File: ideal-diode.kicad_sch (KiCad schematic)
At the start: 6 parts, among them Q1 SIS472DN-T1-GE3, U6 LM74700QDBVRQ1

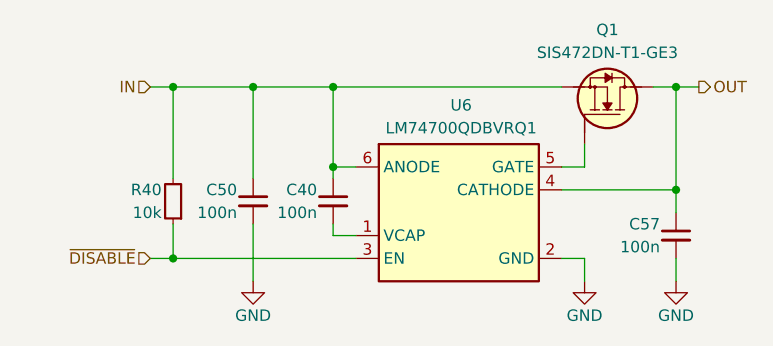
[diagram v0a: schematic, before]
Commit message: [#3] WIP: Clear ERC, re-annotate schematic
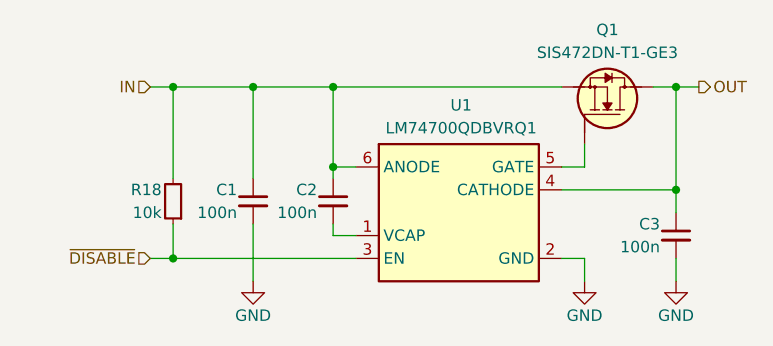
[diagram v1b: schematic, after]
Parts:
- U1: renamed from U6; Manufacturer FTDI Chip -> Texas Instruments
- renumbered C50 to C1, C40 to C2, C57 to C3, R40 to R18
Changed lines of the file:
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@@
 				)
 				(path "/090a8e41-87a8-4fb1-998b-60a2c0dc4cee/1a7e8e9e-4938-4afe-9bd8-99b5f46ce255/e1a72d8b-1f32-454e-9b3f-c70db5c18468"
-					(reference "Q2")
+					(reference "Q3")
 					(unit 1)
 				)
@@
 		(on_board yes)
 		(dnp no)
-		(property "Reference" "#PWR0107"
+		(property "Reference" "#PWR032"
 			(at 127 118.11 0)
 			(effects
@@
 			(project "cm5-module"
 				(path "/090a8e41-87a8-4fb1-998b-60a2c0dc4cee/1a7e8e9e-4938-4afe-9bd8-99b5f46ce255/08db41c3-6072-4efd-8ef3-93ca0731ae13"
-					(reference "#PWR0119")
+					(reference "#PWR0151")
 					(unit 1)
 				)
 				(path "/090a8e41-87a8-4fb1-998b-60a2c0dc4cee/1a7e8e9e-4938-4afe-9bd8-99b5f46ce255/5294994f-978a-402b-88d5-51652b617c01"
-					(reference "#PWR0107")
+					(reference "#PWR032")
 					(unit 1)
 				)
 				(path "/090a8e41-87a8-4fb1-998b-60a2c0dc4cee/1a7e8e9e-4938-4afe-9bd8-99b5f46ce255/e1a72d8b-1f32-454e-9b3f-c70db5c18468"
-					(reference "#PWR0118")
+					(reference "#PWR0141")
 					(unit 1)
 				)
@@
 		(on_board yes)
 		(dnp no)
-		(property "Reference" "C50"
+		(property "Reference" "C1"
 			(at 125.222 101.6 90)
 			(effects
@@
 			(project "cm5-module"
 				(path "/090a8e41-87a8-4fb1-998b-60a2c0dc4cee/1a7e8e9e-4938-4afe-9bd8-99b5f46ce255/08db41c3-6072-4efd-8ef3-93ca0731ae13"
+					(reference "C61")
+					(unit 1)
+				)
+				(path "/090a8e41-87a8-4fb1-998b-60a2c0dc4cee/1a7e8e9e-4938-4afe-9bd8-99b5f46ce255/5294994f-978a-402b-88d5-51652b617c01"
+					(reference "C1")
+					(unit 1)
+				)
+				(path "/090a8e41-87a8-4fb1-998b-60a2c0dc4cee/1a7e8e9e-4938-4afe-9bd8-99b5f46ce255/e1a72d8b-1f32-454e-9b3f-c70db5c18468"
 					(reference "C56")
-					(unit 1)
-				)
-				(path "/090a8e41-87a8-4fb1-998b-60a2c0dc4cee/1a7e8e9e-4938-4afe-9bd8-99b5f46ce255/5294994f-978a-402b-88d5-51652b617c01"
-					(reference "C50")
-					(unit 1)
-				)
-				(path "/090a8e41-87a8-4fb1-998b-60a2c0dc4cee/1a7e8e9e-4938-4afe-9bd8-99b5f46ce255/e1a72d8b-1f32-454e-9b3f-c70db5c18468"
-					(reference "C55")
 					(unit 1)
 				)
@@
 		(on_board yes)
 		(dnp no)
-		(property "Reference" "C40"
+		(property "Reference" "C2"
 			(at 134.112 101.6 90)
 			(effects
@@
 			(project "cm5-module"
 				(path "/090a8e41-87a8-4fb1-998b-60a2c0dc4cee/1a7e8e9e-4938-4afe-9bd8-99b5f46ce255/08db41c3-6072-4efd-8ef3-93ca0731ae13"
-					(reference "C49")
+					(reference "C62")
 					(unit 1)
 				)
 				(path "/090a8e41-87a8-4fb1-998b-60a2c0dc4cee/1a7e8e9e-4938-4afe-9bd8-99b5f46ce255/5294994f-978a-402b-88d5-51652b617c01"
-					(reference "C40")
+					(reference "C2")
 					(unit 1)
 				)
 				(path "/090a8e41-87a8-4fb1-998b-60a2c0dc4cee/1a7e8e9e-4938-4afe-9bd8-99b5f46ce255/e1a72d8b-1f32-454e-9b3f-c70db5c18468"
-					(reference "C41")
+					(reference "C57")
 					(unit 1)
 				)
@@
 		(on_board yes)
 		(dnp no)
-		(property "Reference" "C57"
+		(property "Reference" "C3"
 			(at 172.212 105.41 90)
 			(effects
@@
 			(project "cm5-module"
 				(path "/090a8e41-87a8-4fb1-998b-60a2c0dc4cee/1a7e8e9e-4938-4afe-9bd8-99b5f46ce255/08db41c3-6072-4efd-8ef3-93ca0731ae13"
-					(reference "C59")
+					(reference "C63")
 					(unit 1)
 				)
 				(path "/090a8e41-87a8-4fb1-998b-60a2c0dc4cee/1a7e8e9e-4938-4afe-9bd8-99b5f46ce255/5294994f-978a-402b-88d5-51652b617c01"
-					(reference "C57")
+					(reference "C3")
 					(unit 1)
 				)
@@
 		(on_board yes)
 		(dnp no)
-		(property "Reference" "U6"
+		(property "Reference" "U1"
 			(at 150.114 92.202 0)
 			(effects
@@
 			)
 		)
-		(property "Description" "USB to UART QFN-16-EP(4x4) USB Converters ROHS"
+		(property "Description" "Low IQ Battery Reverse Protection Ideal Diode Controller"
 			(at 173.99 109.22 0)
 			(effects
@@
 			)
 		)
-		(property "Manufacturer" "FTDI Chip"
+		(property "Manufacturer" "Texas Instruments"
 			(at 173.99 111.76 0)
 			(effects
@@
 				)
 				(path "/090a8e41-87a8-4fb1-998b-60a2c0dc4cee/1a7e8e9e-4938-4afe-9bd8-99b5f46ce255/5294994f-978a-402b-88d5-51652b617c01"
-					(reference "U6")
+					(reference "U1")
 					(unit 1)
 				)
 				(path "/090a8e41-87a8-4fb1-998b-60a2c0dc4cee/1a7e8e9e-4938-4afe-9bd8-99b5f46ce255/e1a72d8b-1f32-454e-9b3f-c70db5c18468"
-					(reference "U8")
+					(reference "U10")
 					(unit 1)
 				)
@@
 		(on_board yes)
 		(dnp no)
-		(property "Reference" "R40"
+		(property "Reference" "R18"
 			(at 116.84 101.6 90)
 			(effects
@@
 			(project "cm5-module"
 				(path "/090a8e41-87a8-4fb1-998b-60a2c0dc4cee/1a7e8e9e-4938-4afe-9bd8-99b5f46ce255/08db41c3-6072-4efd-8ef3-93ca0731ae13"
-					(reference "R45")
+					(reference "R64")
 					(unit 1)
 				)
 				(path "/090a8e41-87a8-4fb1-998b-60a2c0dc4cee/1a7e8e9e-4938-4afe-9bd8-99b5f46ce255/5294994f-978a-402b-88d5-51652b617c01"
-					(reference "R40")
+					(reference "R18")
 					(unit 1)
 				)
 				(path "/090a8e41-87a8-4fb1-998b-60a2c0dc4cee/1a7e8e9e-4938-4afe-9bd8-99b5f46ce255/e1a72d8b-1f32-454e-9b3f-c70db5c18468"
-					(reference "R41")
+					(reference "R61")
 					(unit 1)
 				)
@@
 		(on_board yes)
 		(dnp no)
-		(property "Reference" "#PWR0120"
+		(property "Reference" "#PWR034"
 			(at 173.99 118.11 0)
 			(effects
@@
 			(project "cm5-module"
 				(path "/090a8e41-87a8-4fb1-998b-60a2c0dc4cee/1a7e8e9e-4938-4afe-9bd8-99b5f46ce255/08db41c3-6072-4efd-8ef3-93ca0731ae13"
-					(reference "#PWR0129")
+					(reference "#PWR0153")
 					(unit 1)
 				)
 				(path "/090a8e41-87a8-4fb1-998b-60a2c0dc4cee/1a7e8e9e-4938-4afe-9bd8-99b5f46ce255/5294994f-978a-402b-88d5-51652b617c01"
-					(reference "#PWR0120")
+					(reference "#PWR034")
 					(unit 1)
 				)
 				(path "/090a8e41-87a8-4fb1-998b-60a2c0dc4cee/1a7e8e9e-4938-4afe-9bd8-99b5f46ce255/e1a72d8b-1f32-454e-9b3f-c70db5c18468"
-					(reference "#PWR0128")
+					(reference "#PWR0143")
 					(unit 1)
 				)
@@
 		(on_board yes)
 		(dnp no)
-		(property "Reference" "#PWR095"
+		(property "Reference" "#PWR033"
 			(at 163.83 118.11 0)
 			(effects
@@
 			(project "cm5-module"
 				(path "/090a8e41-87a8-4fb1-998b-60a2c0dc4cee/1a7e8e9e-4938-4afe-9bd8-99b5f46ce255/08db41c3-6072-4efd-8ef3-93ca0731ae13"
-					(reference "#PWR0117")
+					(reference "#PWR0152")
 					(unit 1)
 				)
 				(path "/090a8e41-87a8-4fb1-998b-60a2c0dc4cee/1a7e8e9e-4938-4afe-9bd8-99b5f46ce255/5294994f-978a-402b-88d5-51652b617c01"
-					(reference "#PWR095")
+					(reference "#PWR033")
 					(unit 1)
 				)
 				(path "/090a8e41-87a8-4fb1-998b-60a2c0dc4cee/1a7e8e9e-4938-4afe-9bd8-99b5f46ce255/e1a72d8b-1f32-454e-9b3f-c70db5c18468"
-					(reference "#PWR097")
-					(unit 1)
-				)
+					(reference "#PWR0142")
+					(unit 1)
+				)

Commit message: [#3] Re-annotate schematic
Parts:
- renumbered C1 to C21, C2 to C22, C3 to C23, Q1 to Q2, R18 to R11, U1 to U3
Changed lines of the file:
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@@
 		(on_board yes)
 		(dnp no)
-		(property "Reference" "Q1"
+		(property "Reference" "Q2"
 			(at 166.37 83.82 90)
 			(effects
@@
 				)
 				(path "/090a8e41-87a8-4fb1-998b-60a2c0dc4cee/1a7e8e9e-4938-4afe-9bd8-99b5f46ce255/5294994f-978a-402b-88d5-51652b617c01"
-					(reference "Q1")
+					(reference "Q2")
 					(unit 1)
 				)
@@
 		(on_board yes)
 		(dnp no)
-		(property "Reference" "#PWR032"
+		(property "Reference" "#PWR045"
 			(at 127 118.11 0)
 			(effects
@@
 			(project "cm5-module"
 				(path "/090a8e41-87a8-4fb1-998b-60a2c0dc4cee/1a7e8e9e-4938-4afe-9bd8-99b5f46ce255/08db41c3-6072-4efd-8ef3-93ca0731ae13"
-					(reference "#PWR0151")
+					(reference "#PWR051")
 					(unit 1)
 				)
 				(path "/090a8e41-87a8-4fb1-998b-60a2c0dc4cee/1a7e8e9e-4938-4afe-9bd8-99b5f46ce255/5294994f-978a-402b-88d5-51652b617c01"
-					(reference "#PWR032")
+					(reference "#PWR045")
 					(unit 1)
 				)
 				(path "/090a8e41-87a8-4fb1-998b-60a2c0dc4cee/1a7e8e9e-4938-4afe-9bd8-99b5f46ce255/e1a72d8b-1f32-454e-9b3f-c70db5c18468"
-					(reference "#PWR0141")
+					(reference "#PWR048")
 					(unit 1)
 				)
@@
 		(on_board yes)
 		(dnp no)
-		(property "Reference" "C1"
+		(property "Reference" "C21"
 			(at 125.222 101.6 90)
 			(effects
@@
 			(project "cm5-module"
 				(path "/090a8e41-87a8-4fb1-998b-60a2c0dc4cee/1a7e8e9e-4938-4afe-9bd8-99b5f46ce255/08db41c3-6072-4efd-8ef3-93ca0731ae13"
-					(reference "C61")
+					(reference "C27")
 					(unit 1)
 				)
 				(path "/090a8e41-87a8-4fb1-998b-60a2c0dc4cee/1a7e8e9e-4938-4afe-9bd8-99b5f46ce255/5294994f-978a-402b-88d5-51652b617c01"
-					(reference "C1")
+					(reference "C21")
 					(unit 1)
 				)
 				(path "/090a8e41-87a8-4fb1-998b-60a2c0dc4cee/1a7e8e9e-4938-4afe-9bd8-99b5f46ce255/e1a72d8b-1f32-454e-9b3f-c70db5c18468"
-					(reference "C56")
+					(reference "C24")
 					(unit 1)
 				)
@@
 		(on_board yes)
 		(dnp no)
-		(property "Reference" "C2"
+		(property "Reference" "C22"
 			(at 134.112 101.6 90)
 			(effects
@@
 			(project "cm5-module"
 				(path "/090a8e41-87a8-4fb1-998b-60a2c0dc4cee/1a7e8e9e-4938-4afe-9bd8-99b5f46ce255/08db41c3-6072-4efd-8ef3-93ca0731ae13"
-					(reference "C62")
+					(reference "C28")
 					(unit 1)
 				)
 				(path "/090a8e41-87a8-4fb1-998b-60a2c0dc4cee/1a7e8e9e-4938-4afe-9bd8-99b5f46ce255/5294994f-978a-402b-88d5-51652b617c01"
-					(reference "C2")
+					(reference "C22")
 					(unit 1)
 				)
 				(path "/090a8e41-87a8-4fb1-998b-60a2c0dc4cee/1a7e8e9e-4938-4afe-9bd8-99b5f46ce255/e1a72d8b-1f32-454e-9b3f-c70db5c18468"
-					(reference "C57")
+					(reference "C25")
 					(unit 1)
 				)
@@
 		(on_board yes)
 		(dnp no)
-		(property "Reference" "C3"
+		(property "Reference" "C23"
 			(at 172.212 105.41 90)
 			(effects
@@
 			(project "cm5-module"
 				(path "/090a8e41-87a8-4fb1-998b-60a2c0dc4cee/1a7e8e9e-4938-4afe-9bd8-99b5f46ce255/08db41c3-6072-4efd-8ef3-93ca0731ae13"
-					(reference "C63")
+					(reference "C29")
 					(unit 1)
 				)
 				(path "/090a8e41-87a8-4fb1-998b-60a2c0dc4cee/1a7e8e9e-4938-4afe-9bd8-99b5f46ce255/5294994f-978a-402b-88d5-51652b617c01"
-					(reference "C3")
+					(reference "C23")
 					(unit 1)
 				)
 				(path "/090a8e41-87a8-4fb1-998b-60a2c0dc4cee/1a7e8e9e-4938-4afe-9bd8-99b5f46ce255/e1a72d8b-1f32-454e-9b3f-c70db5c18468"
-					(reference "C58")
+					(reference "C26")
 					(unit 1)
 				)
@@
 		(on_board yes)
 		(dnp no)
-		(property "Reference" "U1"
+		(property "Reference" "U3"
 			(at 150.114 92.202 0)
 			(effects
@@
 			(project "cm5-module"
 				(path "/090a8e41-87a8-4fb1-998b-60a2c0dc4cee/1a7e8e9e-4938-4afe-9bd8-99b5f46ce255/08db41c3-6072-4efd-8ef3-93ca0731ae13"
-					(reference "U12")
+					(reference "U5")
 					(unit 1)
 				)
 				(path "/090a8e41-87a8-4fb1-998b-60a2c0dc4cee/1a7e8e9e-4938-4afe-9bd8-99b5f46ce255/5294994f-978a-402b-88d5-51652b617c01"
-					(reference "U1")
+					(reference "U3")
 					(unit 1)
 				)
 				(path "/090a8e41-87a8-4fb1-998b-60a2c0dc4cee/1a7e8e9e-4938-4afe-9bd8-99b5f46ce255/e1a72d8b-1f32-454e-9b3f-c70db5c18468"
-					(reference "U10")
+					(reference "U4")
 					(unit 1)
 				)
@@
 		(on_board yes)
 		(dnp no)
-		(property "Reference" "R18"
+		(property "Reference" "R11"
 			(at 116.84 101.6 90)
 			(effects
@@
 			(project "cm5-module"
 				(path "/090a8e41-87a8-4fb1-998b-60a2c0dc4cee/1a7e8e9e-4938-4afe-9bd8-99b5f46ce255/08db41c3-6072-4efd-8ef3-93ca0731ae13"
-					(reference "R64")
+					(reference "R13")
 					(unit 1)
 				)
 				(path "/090a8e41-87a8-4fb1-998b-60a2c0dc4cee/1a7e8e9e-4938-4afe-9bd8-99b5f46ce255/5294994f-978a-402b-88d5-51652b617c01"
-					(reference "R18")
+					(reference "R11")
 					(unit 1)
 				)
 				(path "/090a8e41-87a8-4fb1-998b-60a2c0dc4cee/1a7e8e9e-4938-4afe-9bd8-99b5f46ce255/e1a72d8b-1f32-454e-9b3f-c70db5c18468"
-					(reference "R61")
+					(reference "R12")
 					(unit 1)
 				)
@@
 		(on_board yes)
 		(dnp no)
-		(property "Reference" "#PWR034"
+		(property "Reference" "#PWR047"
 			(at 173.99 118.11 0)
 			(effects
@@
 			(project "cm5-module"
 				(path "/090a8e41-87a8-4fb1-998b-60a2c0dc4cee/1a7e8e9e-4938-4afe-9bd8-99b5f46ce255/08db41c3-6072-4efd-8ef3-93ca0731ae13"
-					(reference "#PWR0153")
+					(reference "#PWR053")
 					(unit 1)
 				)
 				(path "/090a8e41-87a8-4fb1-998b-60a2c0dc4cee/1a7e8e9e-4938-4afe-9bd8-99b5f46ce255/5294994f-978a-402b-88d5-51652b617c01"
-					(reference "#PWR034")
+					(reference "#PWR047")
 					(unit 1)
 				)
 				(path "/090a8e41-87a8-4fb1-998b-60a2c0dc4cee/1a7e8e9e-4938-4afe-9bd8-99b5f46ce255/e1a72d8b-1f32-454e-9b3f-c70db5c18468"
-					(reference "#PWR0143")
+					(reference "#PWR050")
 					(unit 1)
 				)
@@
 		(on_board yes)
 		(dnp no)
-		(property "Reference" "#PWR033"
+		(property "Reference" "#PWR046"
 			(at 163.83 118.11 0)
 			(effects
@@
 			(project "cm5-module"
 				(path "/090a8e41-87a8-4fb1-998b-60a2c0dc4cee/1a7e8e9e-4938-4afe-9bd8-99b5f46ce255/08db41c3-6072-4efd-8ef3-93ca0731ae13"
-					(reference "#PWR0152")
+					(reference "#PWR052")
 					(unit 1)
 				)
 				(path "/090a8e41-87a8-4fb1-998b-60a2c0dc4cee/1a7e8e9e-4938-4afe-9bd8-99b5f46ce255/5294994f-978a-402b-88d5-51652b617c01"
-					(reference "#PWR033")
+					(reference "#PWR046")
 					(unit 1)
 				)
 				(path "/090a8e41-87a8-4fb1-998b-60a2c0dc4cee/1a7e8e9e-4938-4afe-9bd8-99b5f46ce255/e1a72d8b-1f32-454e-9b3f-c70db5c18468"
-					(reference "#PWR0142")
-					(unit 1)
-				)
+					(reference "#PWR049")
+					(unit 1)
+				)
